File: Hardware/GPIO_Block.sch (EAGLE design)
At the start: 12 parts, among them U2 EDISON_CONNECTOR_FULLMOUNTING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, U3 EDISON_CONNECTOR_FULLHEADER

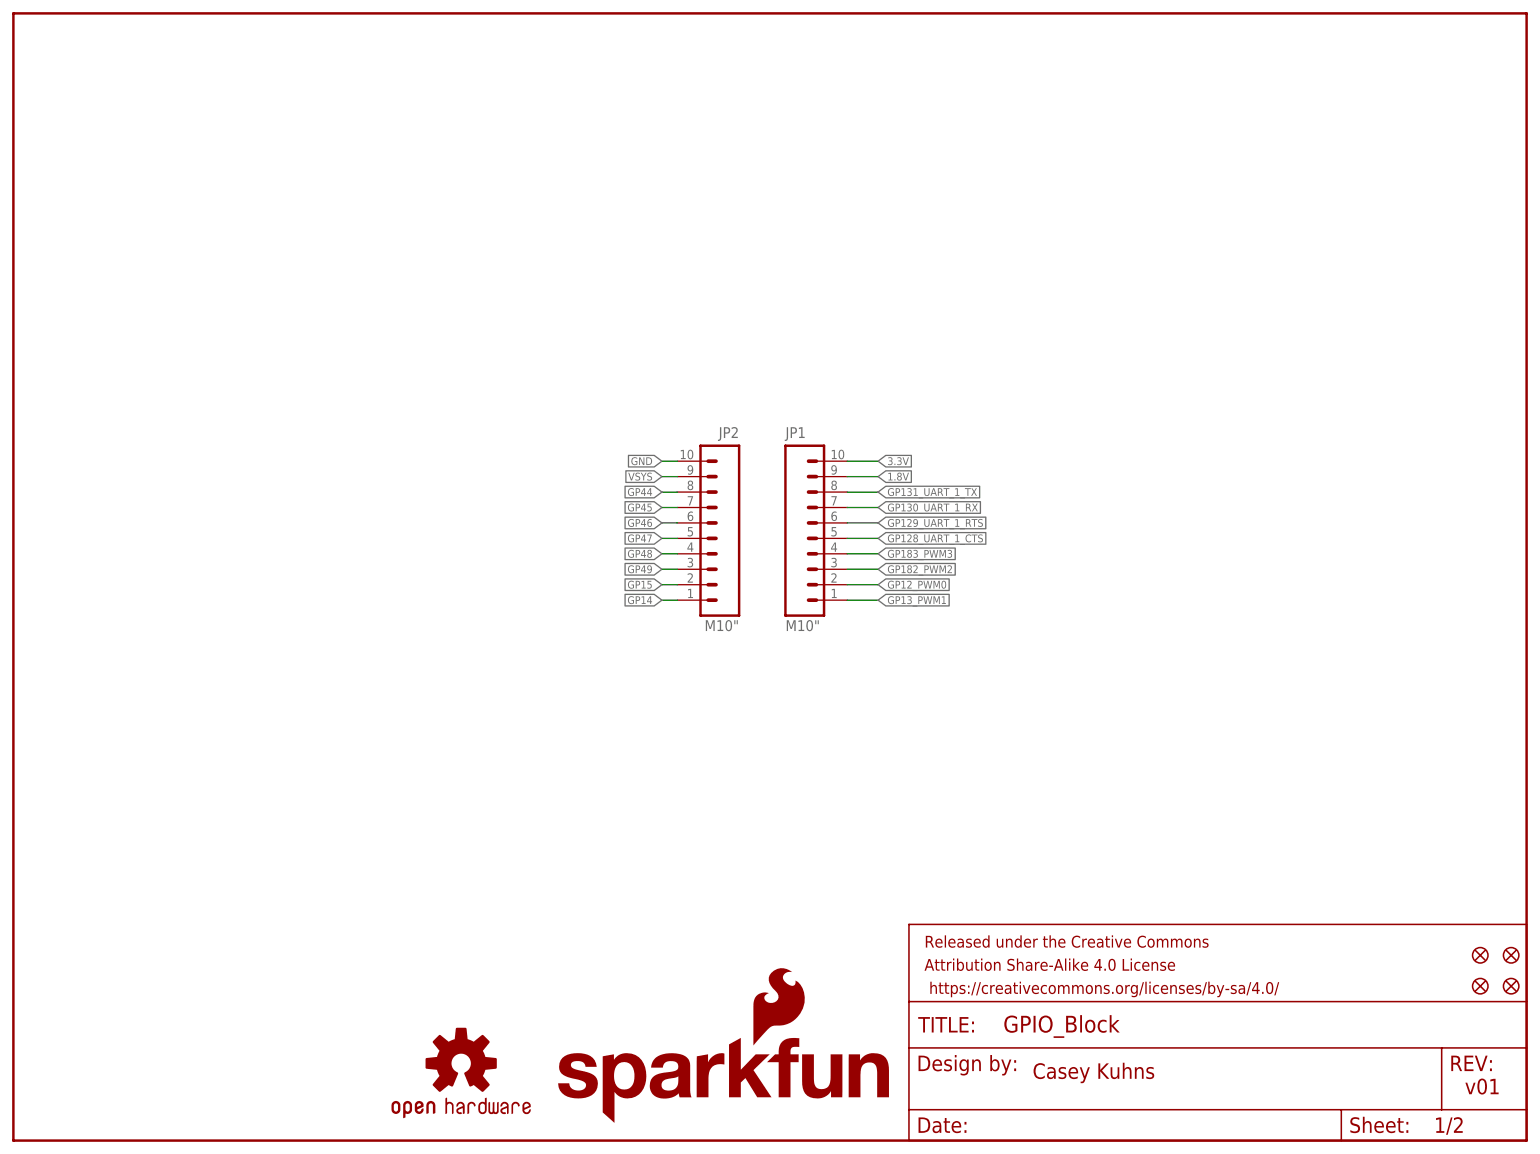
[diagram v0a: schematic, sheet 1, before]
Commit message: added level shifters with the ability to select from vsys and 3.3v cleaned up copper pours changed name on board and files added DCIN pin cleaned up units of board.
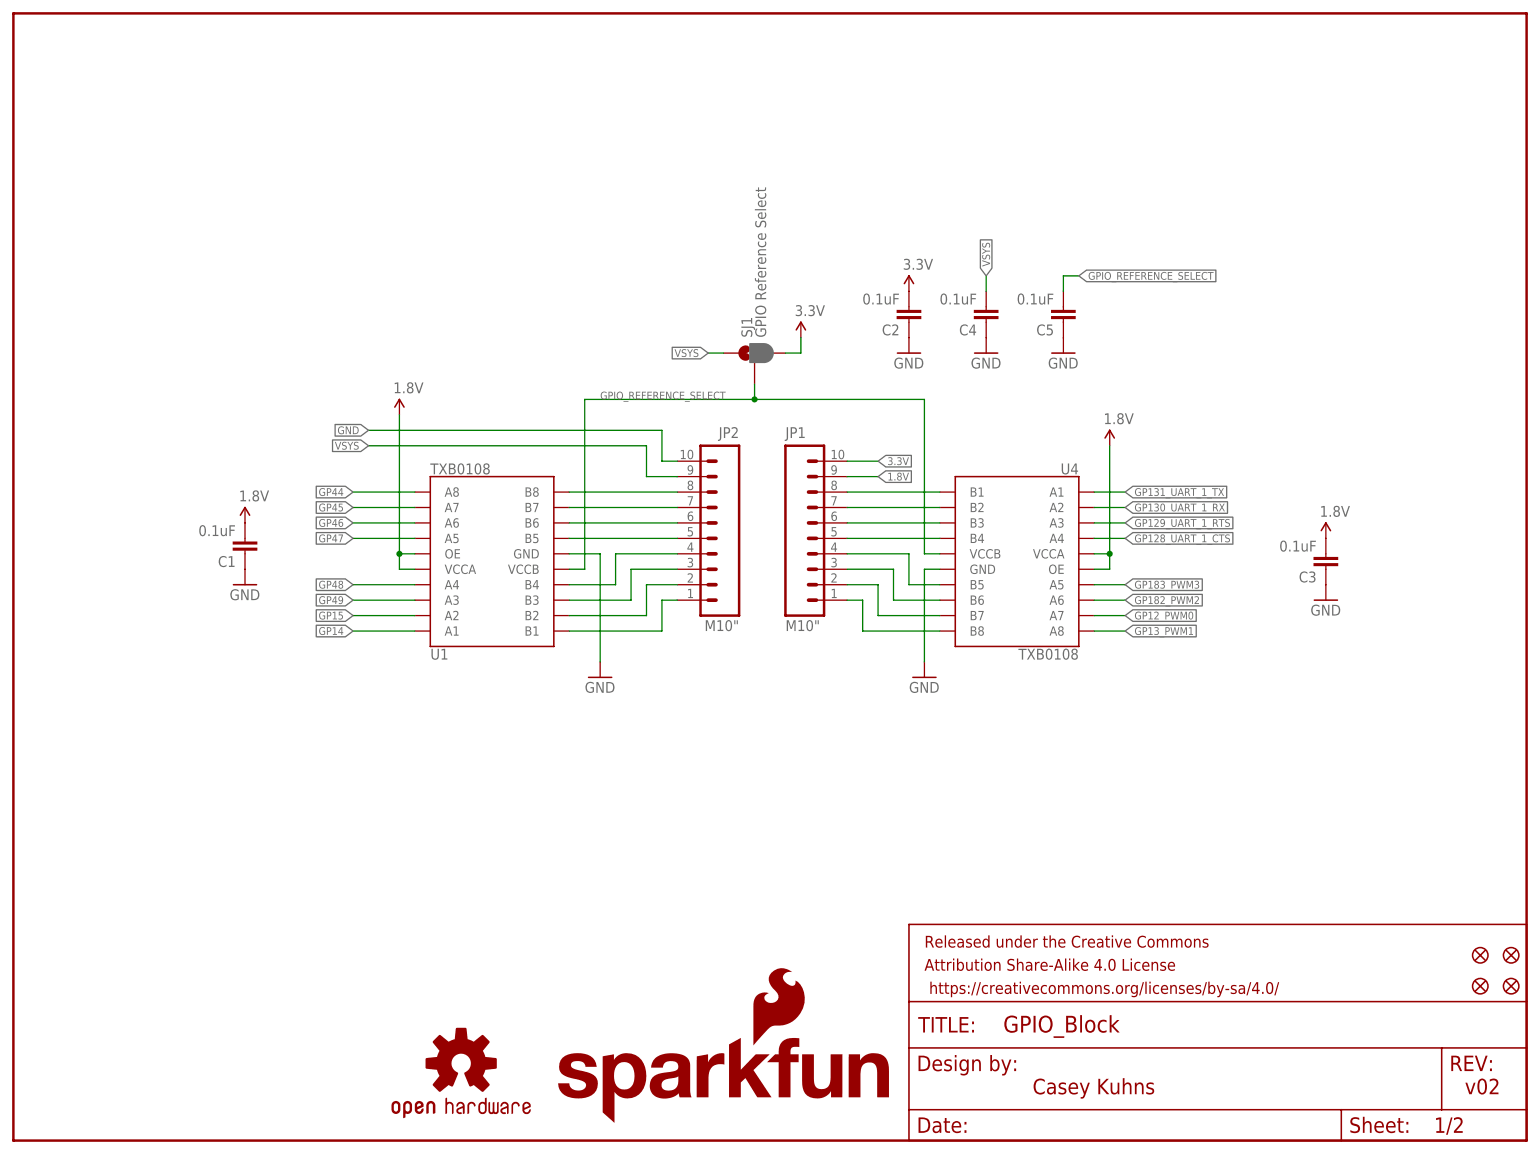
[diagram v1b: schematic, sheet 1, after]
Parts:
- added C1, C2, C3, C4, C5: 0.1uF, SparkFun-Capacitors:0.1UF-25V(+80/-20%)(0603)
- added SJ1: GPIO Reference Select, SparkFun-Passives:JUMPER-PAD-3-2OF3_NC_BY_PASTE
- added U1, U4: TXB0108, Testing:TXB0108
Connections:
- new net DCIN: U2.DCIN, U3.DCIN
- new net GPIO_REFERENCE_SELECT: C5.2, SJ1.2, U1.VCCB, U4.VCCB
- new net N$1: JP2.8, U1.B8
- new net N$11: JP1.4, U4.B5
- new net N$12: JP1.3, U4.B6
- new net N$13: JP1.2, U4.B7
- new net N$14: JP1.1, U4.B8
- new net N$15: JP1.5, U4.B4
- new net N$16: JP1.6, U4.B3
- new net N$17: JP1.7, U4.B2
- new net N$18: JP1.8, U4.B1
- new net N$2: JP2.7, U1.B7
- new net N$3: JP2.6, U1.B6
- new net N$4: JP2.5, U1.B5
- new net N$5: JP2.4, U1.B4
- new net N$6: JP2.3, U1.B3
- new net N$7: JP2.2, U1.B2
- new net N$8: JP2.1, U1.B1
- net 1.8V: now also C1.2, C3.2, U1.OE, U1.VCCA, U4.OE, U4.VCCA
- net 3.3V: now also C2.2, SJ1.3
- net GND: now also C1.1, C2.1, C3.1, C4.1, C5.1, U1.GND, U4.GND
- net GP128_UART_1_CTS: now also U4.A4; no longer JP1.5
- net GP129_UART_1_RTS: now also U4.A3; no longer JP1.6
- net GP12_PWM0: now also U4.A7; no longer JP1.2
- net GP130_UART_1_RX: now also U4.A2; no longer JP1.7
- net GP131_UART_1_TX: now also U4.A1; no longer JP1.8
- net GP13_PWM1: now also U4.A8; no longer JP1.1
- net GP14: now also U1.A1; no longer JP2.1
- net GP15: now also U1.A2; no longer JP2.2
- net GP182_PWM2: now also U4.A6; no longer JP1.3
- net GP183_PWM3: now also U4.A5; no longer JP1.4
- net GP44: now also U1.A8; no longer JP2.8
- net GP45: now also U1.A7; no longer JP2.7
- net GP46: now also U1.A6; no longer JP2.6
- net GP47: now also U1.A5; no longer JP2.5
- net GP48: now also U1.A4; no longer JP2.4
- net GP49: now also U1.A3; no longer JP2.3
- net VSYS: now also C4.2, SJ1.1
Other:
- note added: "v02"
- note removed: "v01"
